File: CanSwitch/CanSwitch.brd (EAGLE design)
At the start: 64.8 x 80 mm, 17 parts

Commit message: swapped proper package for capacitor and also updated library components and little tweaks to the wires
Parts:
- C1, C2, C3, C7, CXT1, CXT2: device rcl:C0805 -> rcl:C025-025X050
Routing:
- net GND: track 181.7 -> 180.8 mm
- net +5V: track 85.1 -> 84.2 mm

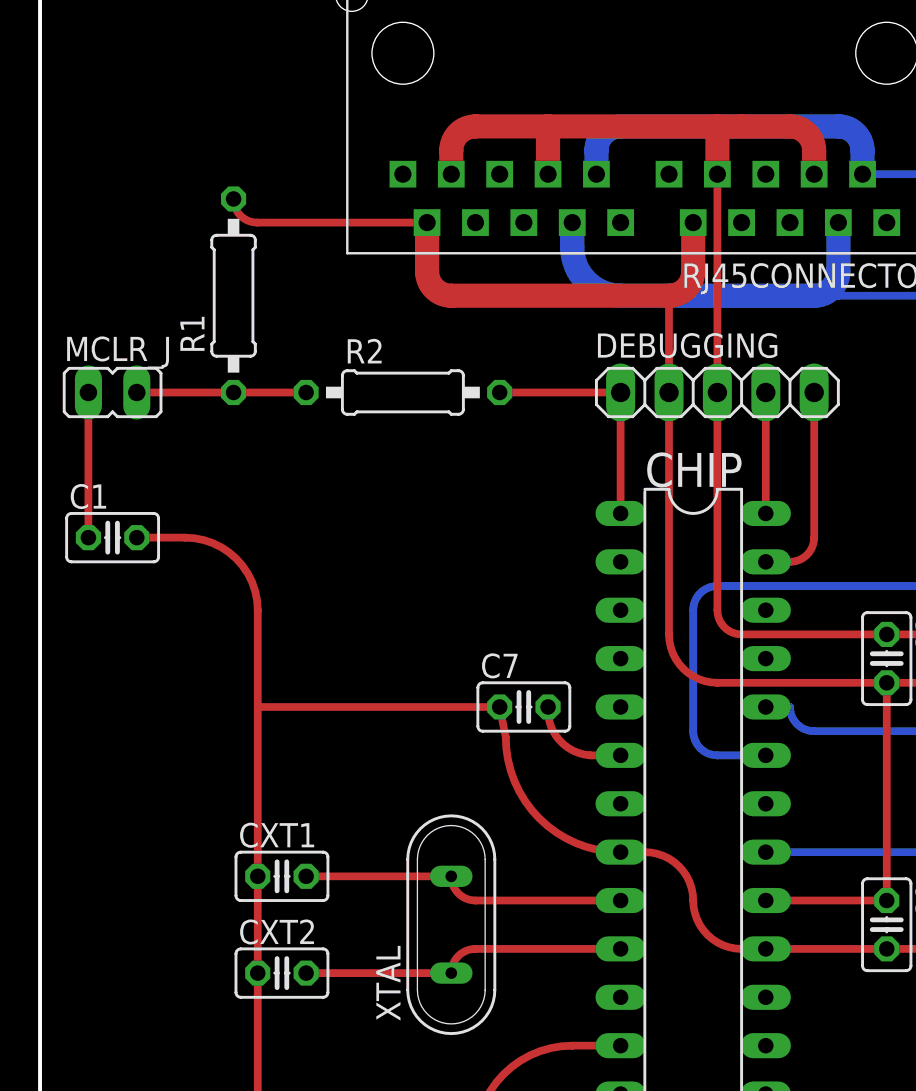
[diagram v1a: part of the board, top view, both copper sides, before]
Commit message: modified components around MCLR to be closer to the pin itself
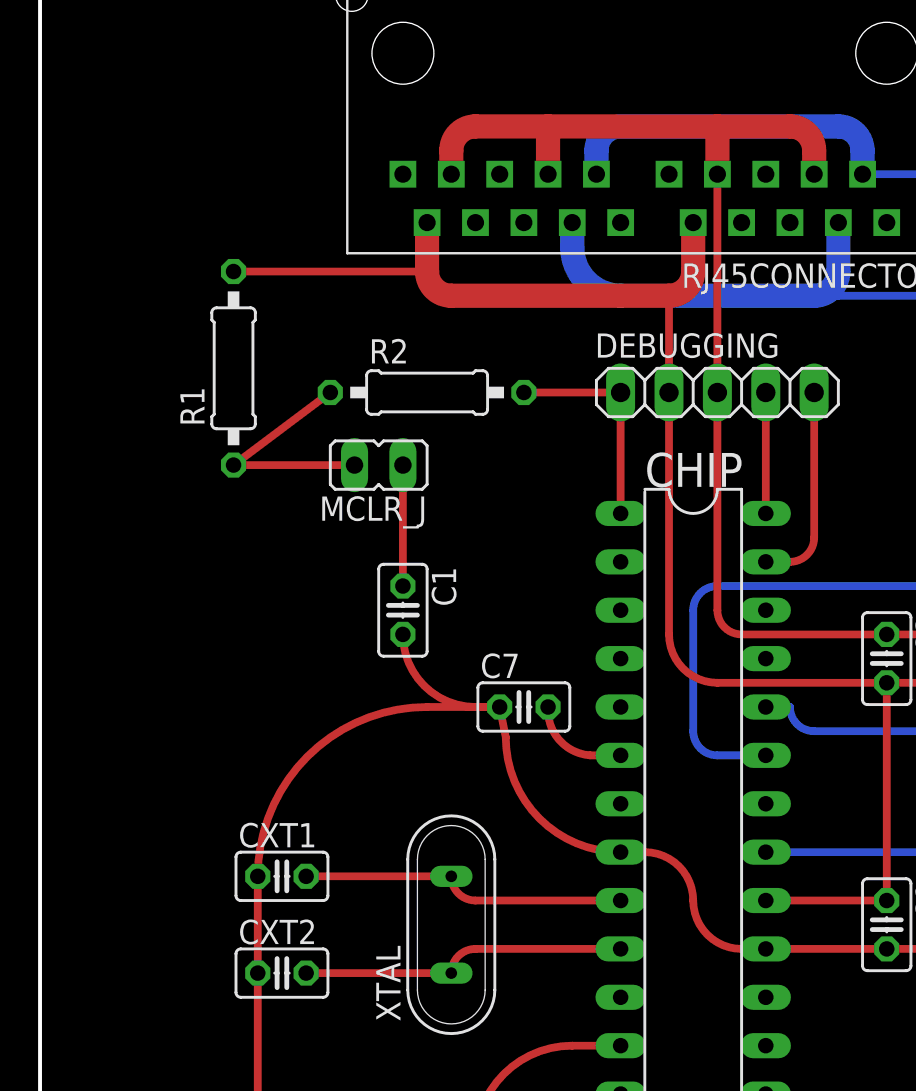
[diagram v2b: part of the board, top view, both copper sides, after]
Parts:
- moved C1 15.7 mm to (38.1, 40.6), turned to 270 degrees
- moved MCLR_J 14.5 mm to (36.8, 48.3), turned to 90 degrees
- moved R1 3.81 mm to (29.2, 53.3)
- moved R2 1.27 mm to (39.4, 52.1)
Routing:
- net GND: track 180.8 -> 168.9 mm
- net N$2: track 8.89 -> 12.7 mm
- net MCLR: track 12.7 -> 11.4 mm
- net N$1: track 7.62 -> 6.35 mm
- net +5V: track 84.2 -> 83.7 mm
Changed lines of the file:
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@@
 </autorouter>
 <elements>
-<element name="C1" library="rcl" package="C025-025X050" value="0.1uF" x="22.86" y="44.45"/>
+<element name="C1" library="rcl" package="C025-025X050" value="0.1uF" x="38.1" y="40.64" rot="R270"/>
 <element name="C2" library="rcl" package="C025-025X050" value="0.1uF" x="63.5" y="24.13" rot="R270"/>
 <element name="C7" library="rcl" package="C025-025X050" value="10 uF" x="44.45" y="35.56"/>
@@
 <element name="CXT2" library="rcl" package="C025-025X050" value="33pF" x="31.75" y="21.59"/>
 <element name="DEBUGGING" library="pinhead" package="1X05" value="" x="54.61" y="52.07"/>
-<element name="MCLR_J" library="jumper" package="JP1" value="" x="22.86" y="52.07" rot="R270"/>
+<element name="MCLR_J" library="jumper" package="JP1" value="" x="36.83" y="48.26" rot="R90"/>
 <element name="MCP2561" library="PoJD" package="MCP2561_PDIP" value="MCP2561MCP" x="72.39" y="38.1"/>
-<element name="R1" library="rcl" package="0207/10" value="10kOhm" x="29.21" y="57.15" rot="R90"/>
-<element name="R2" library="rcl" package="0207/10" value="470Ohm" x="38.1" y="52.07"/>
+<element name="R1" library="rcl" package="0207/10" value="10kOhm" x="29.21" y="53.34" rot="R90"/>
+<element name="R2" library="rcl" package="0207/10" value="470Ohm" x="39.37" y="52.07"/>
 <element name="R3" library="rcl" package="0207/10" value="1kOhm" x="41.91" y="7.62" rot="R90"/>
 <element name="RJ45CONNECTOR" library="PoJD" package="WEBP88_RJ45" value="WEBP88GME" x="50.8" y="68.58" rot="R180"/>
@@
 <contactref element="C3" pad="2"/>
 <wire x1="63.5" y1="36.83" x2="63.5" y2="25.4" width="0.4064" layer="1"/>
-<wire x1="29.21" y1="62.23" x2="30.45" y2="60.99" width="0.4064" layer="1" curve="90"/>
-<wire x1="30.45" y1="60.99" x2="39.37" y2="60.99" width="0.4064" layer="1"/>
 <wire x1="52.07" y1="52.07" x2="52.07" y2="39.37" width="0.4064" layer="1"/>
 <wire x1="52.07" y1="39.37" x2="54.61" y2="36.83" width="0.4064" layer="1" curve="90"/>
@@
 <wire x1="63.5" y1="25.4" x2="57.15" y2="25.4" width="0.4064" layer="1"/>
 <wire x1="68.07" y1="37.15" x2="68.39" y2="36.83" width="0.4064" layer="1" curve="-90"/>
+<wire x1="39.37" y1="58.42" x2="29.21" y2="58.42" width="0.4064" layer="1"/>
 </signal>
 <signal name="GND">
@@
 <wire x1="41.91" y1="66.04" x2="45.72" y2="66.04" width="1.27" layer="1"/>
 <wire x1="45.72" y1="66.04" x2="54.61" y2="66.04" width="1.27" layer="1"/>
-<wire x1="55.88" y1="66.04" x2="58.42" y2="66.04" width="1.27" layer="1"/>
+<wire x1="54.61" y1="66.04" x2="58.42" y2="66.04" width="1.27" layer="1"/>
 <wire x1="59.69" y1="63.53" x2="59.69" y2="64.77" width="1.27" layer="1"/>
 <wire x1="59.69" y1="64.77" x2="58.42" y2="66.04" width="1.27" layer="1" curve="90"/>
@@
 <wire x1="30.48" y1="5.08" x2="30.48" y2="21.27" width="0.4064" layer="1"/>
 <wire x1="30.48" y1="21.27" x2="30.48" y2="21.59" width="0.4064" layer="1" curve="-90"/>
-<wire x1="30.48" y1="21.59" x2="30.48" y2="26.35" width="0.4064" layer="1"/>
-<wire x1="30.48" y1="26.35" x2="30.48" y2="26.67" width="0.4064" layer="1" curve="-90"/>
-<wire x1="24.13" y1="44.45" x2="26.67" y2="44.45" width="0.4064" layer="1"/>
-<wire x1="26.67" y1="44.45" x2="30.48" y2="40.64" width="0.4064" layer="1" curve="-90"/>
-<wire x1="30.48" y1="40.64" x2="30.48" y2="35.56" width="0.4064" layer="1"/>
-<wire x1="30.48" y1="35.56" x2="30.48" y2="26.99" width="0.4064" layer="1"/>
-<wire x1="30.48" y1="26.99" x2="30.48" y2="26.67" width="0.4064" layer="1" curve="90"/>
-<wire x1="30.48" y1="26.67" x2="30.48" y2="26.99" width="0.4064" layer="1"/>
-<wire x1="30.48" y1="35.56" x2="43.18" y2="35.56" width="0.4064" layer="1"/>
 <wire x1="63.5" y1="22.86" x2="71.16" y2="22.86" width="0.4064" layer="1"/>
 <wire x1="71.16" y1="22.86" x2="71.16" y2="23.8" width="0.4064" layer="1"/>
 <wire x1="45.72" y1="63.53" x2="45.72" y2="66.04" width="1.27" layer="1"/>
 <wire x1="54.61" y1="63.53" x2="54.61" y2="66.04" width="1.27" layer="1"/>
-<wire x1="55.88" y1="66.04" x2="54.61" y2="66.04" width="1.27" layer="1"/>
+<wire x1="38.1" y1="39.37" x2="41.91" y2="35.56" width="0.4064" layer="1" curve="90"/>
+<wire x1="41.91" y1="35.56" x2="43.18" y2="35.56" width="0.4064" layer="1"/>
+<wire x1="30.48" y1="26.67" x2="39.37" y2="35.56" width="0.4064" layer="1" curve="-90"/>
+<wire x1="39.37" y1="35.56" x2="43.18" y2="35.56" width="0.4064" layer="1"/>
+<wire x1="30.48" y1="26.67" x2="30.48" y2="21.59" width="0.4064" layer="1"/>
 </signal>
 <signal name="N$2">
@@
 <contactref element="MCLR_J" pad="2"/>
 <contactref element="R2" pad="1"/>
-<wire x1="33.02" y1="52.07" x2="29.21" y2="52.07" width="0.4064" layer="1"/>
-<wire x1="29.21" y1="52.07" x2="24.13" y2="52.07" width="0.4064" layer="1"/>
+<wire x1="34.29" y1="52.07" x2="29.21" y2="48.26" width="0.4064" layer="1"/>
+<wire x1="29.21" y1="48.26" x2="35.56" y2="48.26" width="0.4064" layer="1"/>
 </signal>
 <signal name="MCLR">
@@
 <contactref element="CHIP" pad="1"/>
 <wire x1="49.53" y1="52.07" x2="49.53" y2="45.72" width="0.4064" layer="1"/>
-<wire x1="43.18" y1="52.07" x2="49.53" y2="52.07" width="0.4064" layer="1"/>
+<wire x1="44.45" y1="52.07" x2="49.53" y2="52.07" width="0.4064" layer="1"/>
 </signal>
 <signal name="N$1">
 <contactref element="C1" pad="1"/>
 <contactref element="MCLR_J" pad="1"/>
-<wire x1="21.59" y1="52.07" x2="21.59" y2="44.45" width="0.4064" layer="1"/>
+<wire x1="38.1" y1="48.26" x2="38.1" y2="41.91" width="0.4064" layer="1"/>
 </signal>
 <signal name="N$4">

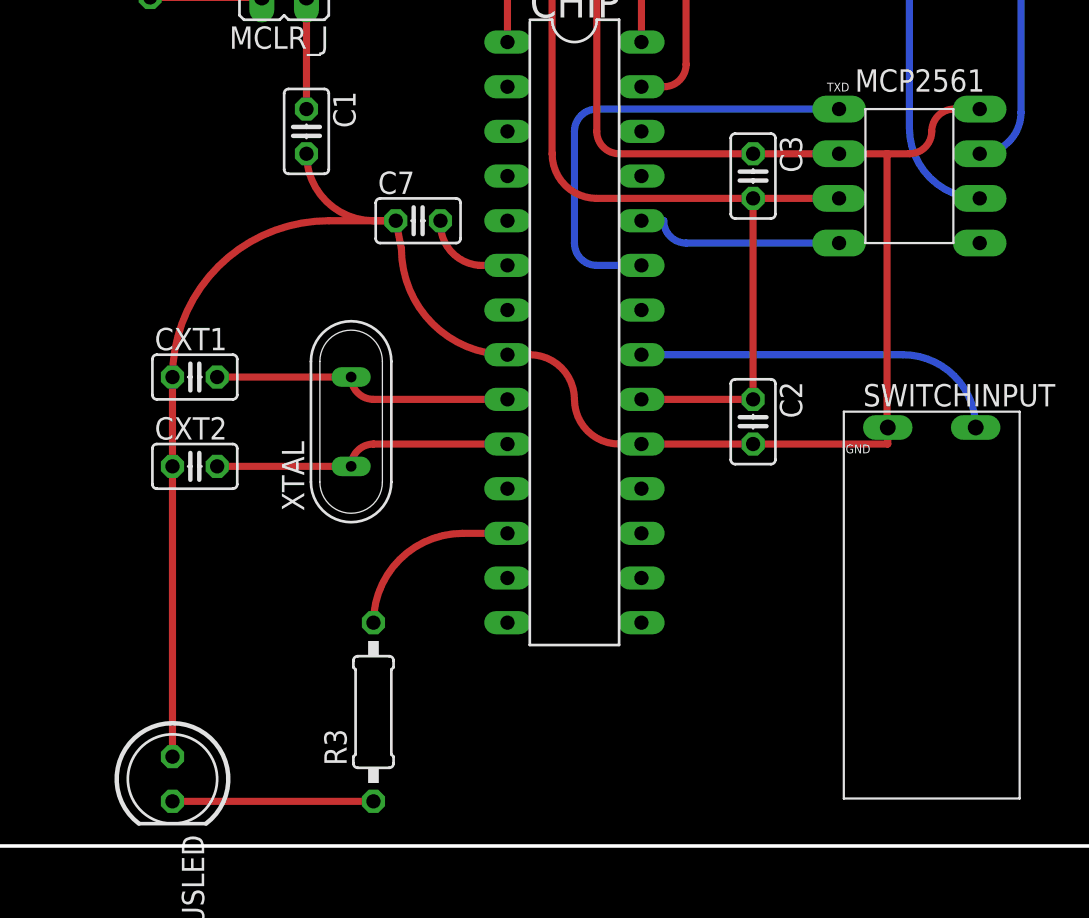
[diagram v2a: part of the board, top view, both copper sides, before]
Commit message: #1 added grounded copper pour around XTAL and chips
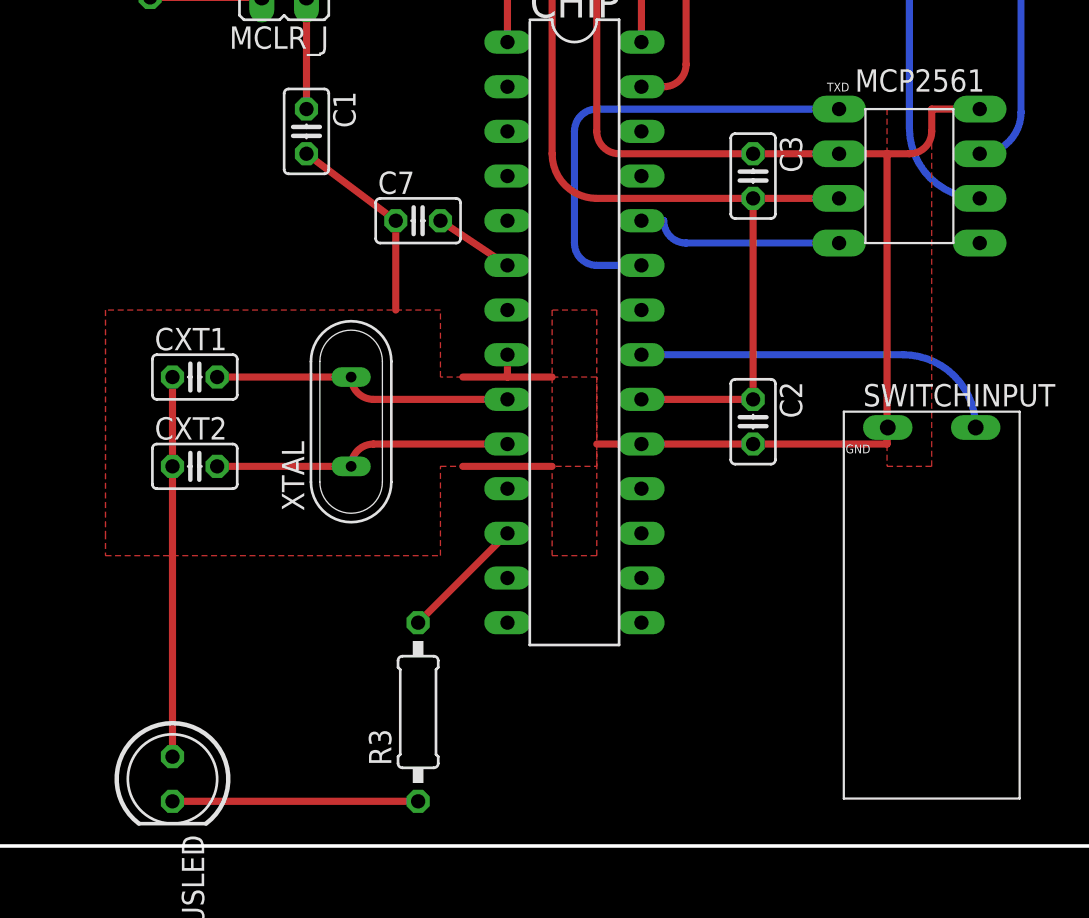
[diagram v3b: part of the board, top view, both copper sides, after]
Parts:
- moved R3 2.54 mm to (44.5, 7.62)
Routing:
- net GND: track 168.9 -> 152.1 mm
- net N$8: track 11.4 -> 14.0 mm
- net N$7: track 9.72 -> 7.18 mm
- added copper zone on layer 1, net GND
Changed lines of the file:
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@@
 <element name="R1" library="rcl" package="0207/10" value="10kOhm" x="29.21" y="53.34" rot="R90"/>
 <element name="R2" library="rcl" package="0207/10" value="470Ohm" x="39.37" y="52.07"/>
-<element name="R3" library="rcl" package="0207/10" value="1kOhm" x="41.91" y="7.62" rot="R90"/>
+<element name="R3" library="rcl" package="0207/10" value="1kOhm" x="44.45" y="7.62" rot="R90"/>
 <element name="RJ45CONNECTOR" library="PoJD" package="WEBP88_RJ45" value="WEBP88GME" x="50.8" y="68.58" rot="R180"/>
 <element name="STATUSLED" library="led" package="LED5MM" value="" x="30.48" y="3.81" rot="R270"/>
@@
 <wire x1="59.69" y1="64.77" x2="58.42" y2="66.04" width="1.27" layer="1" curve="90"/>
 <wire x1="54.61" y1="63.53" x2="54.61" y2="52.07" width="0.4064" layer="1"/>
-<wire x1="76.39" y1="41.91" x2="74.93" y2="41.91" width="0.4064" layer="1"/>
-<wire x1="74.93" y1="41.91" x2="73.66" y2="40.64" width="0.4064" layer="1" curve="90"/>
+<wire x1="76.39" y1="41.91" x2="73.66" y2="41.91" width="0.4064" layer="1"/>
 <wire x1="73.66" y1="40.64" x2="72.39" y2="39.37" width="0.4064" layer="1" curve="-90"/>
 <wire x1="72.39" y1="39.37" x2="71.12" y2="39.37" width="0.4064" layer="1"/>
@@
 <wire x1="71.12" y1="39.37" x2="71.12" y2="23.84" width="0.4064" layer="1"/>
 <wire x1="71.12" y1="23.84" x2="71.16" y2="23.8" width="0.4064" layer="1" curve="90"/>
-<wire x1="57.15" y1="22.86" x2="55.88" y2="22.86" width="0.4064" layer="1"/>
-<wire x1="55.88" y1="22.86" x2="53.34" y2="25.4" width="0.4064" layer="1" curve="-90"/>
-<wire x1="53.34" y1="25.4" x2="50.8" y2="27.94" width="0.4064" layer="1" curve="90"/>
-<wire x1="50.8" y1="27.94" x2="49.53" y2="27.94" width="0.4064" layer="1"/>
 <wire x1="54.61" y1="52.07" x2="54.61" y2="40.64" width="0.4064" layer="1"/>
 <wire x1="54.61" y1="40.64" x2="55.88" y2="39.37" width="0.4064" layer="1" curve="90"/>
@@
 <wire x1="57.15" y1="22.86" x2="63.18" y2="22.86" width="0.4064" layer="1"/>
 <wire x1="63.18" y1="22.86" x2="63.5" y2="22.86" width="0.4064" layer="1" curve="90"/>
-<wire x1="43.18" y1="35.56" x2="43.5" y2="33.97" width="0.4064" layer="1"/>
-<wire x1="43.5" y1="33.97" x2="49.53" y2="27.94" width="0.4064" layer="1" curve="90"/>
 <wire x1="30.48" y1="5.08" x2="30.48" y2="21.27" width="0.4064" layer="1"/>
 <wire x1="30.48" y1="21.27" x2="30.48" y2="21.59" width="0.4064" layer="1" curve="-90"/>
-<wire x1="63.5" y1="22.86" x2="71.16" y2="22.86" width="0.4064" layer="1"/>
-<wire x1="71.16" y1="22.86" x2="71.16" y2="23.8" width="0.4064" layer="1"/>
 <wire x1="45.72" y1="63.53" x2="45.72" y2="66.04" width="1.27" layer="1"/>
 <wire x1="54.61" y1="63.53" x2="54.61" y2="66.04" width="1.27" layer="1"/>
-<wire x1="38.1" y1="39.37" x2="41.91" y2="35.56" width="0.4064" layer="1" curve="90"/>
-<wire x1="41.91" y1="35.56" x2="43.18" y2="35.56" width="0.4064" layer="1"/>
-<wire x1="30.48" y1="26.67" x2="39.37" y2="35.56" width="0.4064" layer="1" curve="-90"/>
-<wire x1="39.37" y1="35.56" x2="43.18" y2="35.56" width="0.4064" layer="1"/>
 <wire x1="30.48" y1="26.67" x2="30.48" y2="21.59" width="0.4064" layer="1"/>
+<wire x1="43.18" y1="35.56" x2="43.18" y2="30.48" width="0.4064" layer="1"/>
+<wire x1="38.1" y1="39.37" x2="43.18" y2="35.56" width="0.4064" layer="1"/>
+<polygon width="0.4064" layer="1" isolate="0.6096">
+<vertex x="26.67" y="30.48"/>
+<vertex x="26.67" y="17.78"/>
+<vertex x="26.67" y="16.51"/>
+<vertex x="45.72" y="16.51"/>
+<vertex x="45.72" y="21.59"/>
+<vertex x="54.61" y="21.59"/>
+<vertex x="54.61" y="26.67"/>
+<vertex x="45.72" y="26.67"/>
+<vertex x="45.72" y="30.48"/>
+</polygon>
+<polygon width="0.4064" layer="1" isolate="0.6096">
+<vertex x="52.07" y="30.48"/>
+<vertex x="52.07" y="16.51"/>
+<vertex x="54.61" y="16.51"/>
+<vertex x="54.61" y="30.48"/>
+</polygon>
+<wire x1="57.15" y1="22.86" x2="54.61" y2="22.86" width="0.4064" layer="1"/>
+<wire x1="46.99" y1="26.67" x2="49.53" y2="26.67" width="0.4064" layer="1"/>
+<wire x1="49.53" y1="26.67" x2="52.07" y2="26.67" width="0.4064" layer="1"/>
+<wire x1="46.99" y1="21.59" x2="52.07" y2="21.59" width="0.4064" layer="1"/>
+<wire x1="49.53" y1="27.94" x2="49.53" y2="26.67" width="0.4064" layer="1"/>
+<polygon width="0.4064" layer="1" isolate="0.6096">
+<vertex x="71.12" y="41.91"/>
+<vertex x="71.12" y="21.59"/>
+<vertex x="73.66" y="21.59"/>
+<vertex x="73.66" y="41.91"/>
+</polygon>
+<wire x1="63.5" y1="22.86" x2="71.12" y2="22.86" width="0.4064" layer="1"/>
+<wire x1="71.12" y1="22.86" x2="71.16" y2="23.8" width="0.4064" layer="1"/>
+<wire x1="73.66" y1="41.91" x2="73.66" y2="40.64" width="0.4064" layer="1"/>
 </signal>
 <signal name="N$2">
@@
 <contactref element="CHIP" pad="6"/>
 <contactref element="C7" pad="2"/>
-<wire x1="49.53" y1="33.02" x2="47.94" y2="33.02" width="0.4064" layer="1"/>
-<wire x1="47.94" y1="33.02" x2="45.72" y2="35.56" width="0.4064" layer="1" curve="-90"/>
+<wire x1="49.53" y1="33.02" x2="45.72" y2="35.56" width="0.4064" layer="1"/>
 </signal>
 <signal name="N$6">
@@
 <contactref element="CHIP" pad="12"/>
 <contactref element="R3" pad="2"/>
-<wire x1="41.91" y1="12.7" x2="46.99" y2="17.78" width="0.4064" layer="1" curve="-90"/>
-<wire x1="46.99" y1="17.78" x2="49.53" y2="17.78" width="0.4064" layer="1"/>
+<wire x1="49.53" y1="17.78" x2="44.45" y2="12.7" width="0.4064" layer="1"/>
 </signal>
 <signal name="N$8">
 <contactref element="R3" pad="1"/>
 <contactref element="STATUSLED" pad="K"/>
-<wire x1="41.91" y1="2.54" x2="30.48" y2="2.54" width="0.4064" layer="1"/>
+<wire x1="44.45" y1="2.54" x2="30.48" y2="2.54" width="0.4064" layer="1"/>
 </signal>
 <signal name="INPUT">
